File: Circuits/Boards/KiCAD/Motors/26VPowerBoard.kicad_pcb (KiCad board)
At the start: 2 copper layers, 30.5 x 25.4 mm, 13 parts, among them J1 Conn_01x01, J2 Conn_01x01, J3 Conn_01x01, U1 HCPL063

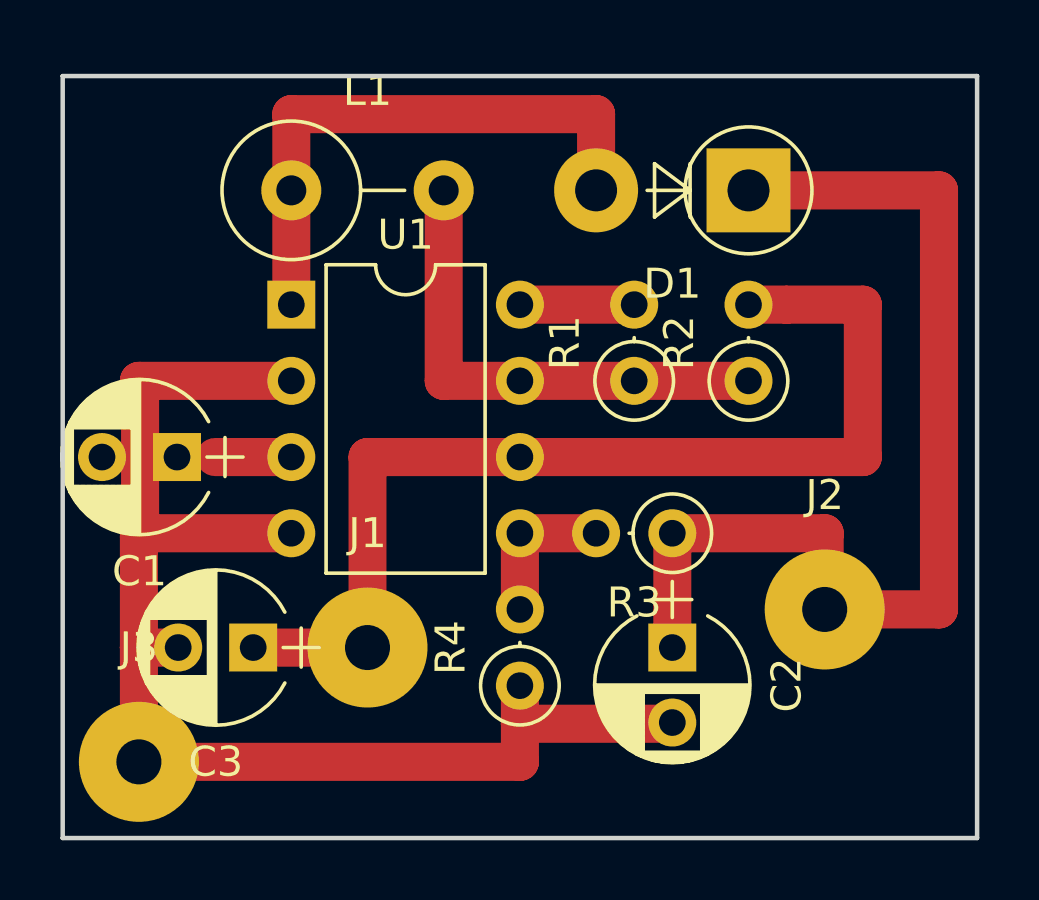
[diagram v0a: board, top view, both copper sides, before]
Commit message: Added 26V and 5V units to the Dual motor controller board
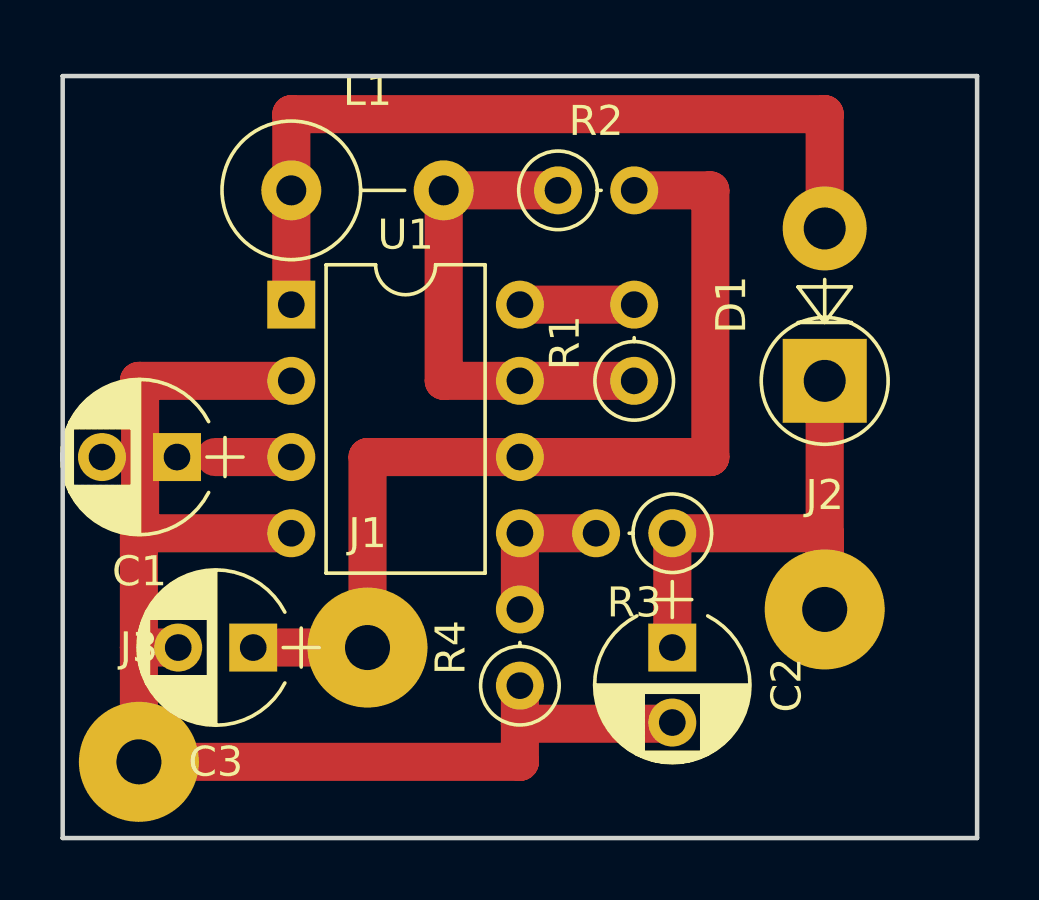
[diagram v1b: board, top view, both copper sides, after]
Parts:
- moved R2 8.98 mm to (120.7, 100.3), turned to 0 degrees
- moved D1 6.84 mm to (129.5, 106.7), turned to 90 degrees
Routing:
- net /VG2: track 35.6 -> 19.0 mm
- net /N$5: track 19.0 -> 27.9 mm
- net /VDD: track 35.6 -> 33.0 mm
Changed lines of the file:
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@@
     (links 21)
     (no_connects 2)
-    (area 104.064999 96.444999 134.695001 121.995001)
+    (area 101.344981 96.0926 134.695001 124.2174)
     (thickness 1.6)
     (drawings 4)
-    (tracks 39)
+    (tracks 36)
     (zones 0)
     (modules 13)
@@
   )
   (setup
-    (last_trace_width 0.8128)
+    (last_trace_width 1.27)
     (user_trace_width 0.1524)
     (user_trace_width 0.8128)
@@
   )
   (module Diodes_THT:D_5W_P5.08mm_Vertical_AnodeUp (layer Top)
-    (at 127 100.33 180)
+    (at 129.54 106.68 90)
     (descr "D, 5W series, Axial, Vertical, pin pitch=5.08mm, , length*diameter=8.9*3.7mm^2, , http://www.diodes.com/_files/packages/8686949.gif")
     (tags "D 5W series Axial Vertical pin pitch 5.08mm  length 8.9mm diameter 3.7mm")
-    (fp_text reference D1 (at 2.54 -3.114899 180) (layer F.SilkS)
-      (effects (font (size 1 1) (thickness 0.15)))
-    )
-    (fp_text value D (at 2.54 3.114899 180) (layer F.Fab)
-      (effects (font (size 1 1) (thickness 0.15)))
-    )
-    (fp_text user K (at -2.814899 0 180) (layer F.Fab)
-      (effects (font (size 1 1) (thickness 0.15)))
-    )
-    (fp_text user %R (at 2.54 0 180) (layer F.Fab)
+    (fp_text reference D1 (at 2.54 -3.114899 90) (layer F.SilkS)
+      (effects (font (size 1 1) (thickness 0.15)))
+    )
+    (fp_text value D (at 2.54 3.114899 90) (layer F.Fab)
+      (effects (font (size 1 1) (thickness 0.15)))
+    )
+    (fp_text user K (at -2.814899 0 90) (layer F.Fab)
+      (effects (font (size 1 1) (thickness 0.15)))
+    )
+    (fp_text user %R (at 2.54 0 90) (layer F.Fab)
       (effects (font (size 1 1) (thickness 0.15)))
     )
@@
     (fp_circle (center 0 0) (end 1.85 0) (layer F.Fab) (width 0.1))
     (fp_circle (center 0 0) (end 2.114899 0) (layer F.SilkS) (width 0.12))
-    (pad 1 thru_hole rect (at 0 0 180) (size 2.8 2.8) (drill 1.4) (layers *.Cu *.Mask)
+    (pad 1 thru_hole rect (at 0 0 90) (size 2.8 2.8) (drill 1.4) (layers *.Cu *.Mask)
       (net 3 /VG2))
-    (pad 2 thru_hole oval (at 5.08 0 180) (size 2.8 2.8) (drill 1.4) (layers *.Cu *.Mask)
+    (pad 2 thru_hole oval (at 5.08 0 90) (size 2.8 2.8) (drill 1.4) (layers *.Cu *.Mask)
       (net 4 /N$5))
     (model ${KISYS3DMOD}/Diodes_THT.3dshapes/D_5W_P5.08mm_Vertical_AnodeUp.wrl
@@
   )
   (module Resistors_THT:R_Axial_DIN0207_L6.3mm_D2.5mm_P2.54mm_Vertical (layer Top)
-    (at 127 106.68 90)
+    (at 120.65 100.33)
     (descr "Resistor, Axial_DIN0207 series, Axial, Vertical, pin pitch=2.54mm, 0.25W = 1/4W, length*diameter=6.3*2.5mm^2, http://cdn-reichelt.de/documents/datenblatt/B400/1_4W%23YAG.pdf")
     (tags "Resistor Axial_DIN0207 series Axial Vertical pin pitch 2.54mm 0.25W = 1/4W length 6.3mm diameter 2.5mm")
-    (fp_text reference R2 (at 1.27 -2.31 90) (layer F.SilkS)
-      (effects (font (size 1 1) (thickness 0.15)))
-    )
-    (fp_text value 0.22 (at 1.27 2.31 90) (layer F.Fab)
+    (fp_text reference R2 (at 1.27 -2.31) (layer F.SilkS)
+      (effects (font (size 1 1) (thickness 0.15)))
+    )
+    (fp_text value 0.22 (at 1.27 2.31) (layer F.Fab)
       (effects (font (size 1 1) (thickness 0.15)))
     )
@@
     (fp_line (start 3.65 1.6) (end 3.65 -1.6) (layer F.CrtYd) (width 0.05))
     (fp_line (start 3.65 -1.6) (end -1.6 -1.6) (layer F.CrtYd) (width 0.05))
-    (pad 1 thru_hole circle (at 0 0 90) (size 1.6 1.6) (drill 0.889) (layers *.Cu *.Mask)
+    (pad 1 thru_hole circle (at 0 0) (size 1.6 1.6) (drill 0.889) (layers *.Cu *.Mask)
       (net 5 /N$12))
-    (pad 2 thru_hole oval (at 2.54 0 90) (size 1.6 1.6) (drill 0.889) (layers *.Cu *.Mask)
+    (pad 2 thru_hole oval (at 2.54 0) (size 1.6 1.6) (drill 0.889) (layers *.Cu *.Mask)
       (net 7 /VDD))
     (model ${KISYS3DMOD}/Resistors_THT.3dshapes/R_Axial_DIN0207_L6.3mm_D2.5mm_P2.54mm_Vertical.wrl
@@
   (segment (start 106.68 106.68) (end 106.72 106.72) (width 1.27) (layer Top) (net 2))
   (segment (start 124.42 118.11) (end 124.46 118.07) (width 1.27) (layer Top) (net 2) (status 30))
-  (segment (start 127 100.33) (end 133.35 100.33) (width 1.27) (layer Top) (net 3) (status 10))
-  (segment (start 133.35 114.3) (end 129.54 114.3) (width 1.27) (layer Top) (net 3))
-  (segment (start 133.35 100.33) (end 133.35 114.3) (width 1.27) (layer Top) (net 3))
+  (segment (start 129.54 106.68) (end 129.54 114.3) (width 1.27) (layer Top) (net 3) (status C00000))
   (segment (start 129.54 114.3) (end 129.54 111.76) (width 1.27) (layer Top) (net 3))
   (segment (start 124.46 111.76) (end 129.54 111.76) (width 1.27) (layer Top) (net 3))
   (segment (start 124.46 111.76) (end 124.46 115.57) (width 1.27) (layer Top) (net 3))
-  (segment (start 111.76 100.33) (end 111.76 97.79) (width 1.27) (layer Top) (net 4))
-  (segment (start 121.92 97.79) (end 121.92 100.33) (width 1.27) (layer Top) (net 4))
-  (segment (start 111.76 97.79) (end 121.92 97.79) (width 1.27) (layer Top) (net 4))
+  (segment (start 111.76 100.33) (end 111.76 97.79) (width 1.27) (layer Top) (net 4) (status 400000))
+  (segment (start 129.54 97.79) (end 129.54 101.6) (width 1.27) (layer Top) (net 4) (status 800000))
+  (segment (start 111.76 97.79) (end 129.54 97.79) (width 1.27) (layer Top) (net 4))
   (segment (start 111.76 104.14) (end 111.76 100.33) (width 1.27) (layer Top) (net 4) (status 20))
+  (segment (start 116.84 100.33) (end 120.65 100.33) (width 1.27) (layer Top) (net 5) (status C00000))
   (segment (start 116.84 100.33) (end 116.84 106.68) (width 1.27) (layer Top) (net 5))
   (segment (start 116.84 106.68) (end 119.38 106.68) (width 1.27) (layer Top) (net 5))
   (segment (start 119.38 106.68) (end 123.19 106.68) (width 1.27) (layer Top) (net 5))
-  (segment (start 127 106.68) (end 123.19 106.68) (width 1.27) (layer Top) (net 5))
   (segment (start 123.19 104.14) (end 119.38 104.14) (width 1.27) (layer Top) (net 6))
+  (segment (start 123.19 100.33) (end 125.73 100.33) (width 1.27) (layer Top) (net 7) (status 400000))
+  (segment (start 125.73 109.22) (end 119.38 109.22) (width 1.27) (layer Top) (net 7) (status 800000))
+  (segment (start 125.73 100.33) (end 125.73 109.22) (width 1.27) (layer Top) (net 7))
   (segment (start 110.49 115.57) (end 114.3 115.57) (width 1.27) (layer Top) (net 7))
   (segment (start 119.38 109.22) (end 114.3 109.22) (width 1.27) (layer Top) (net 7))
   (segment (start 114.3 109.22) (end 114.3 115.57) (width 1.27) (layer Top) (net 7) (status 20))
-  (segment (start 119.38 109.22) (end 130.81 109.22) (width 1.27) (layer Top) (net 7))
-  (segment (start 130.81 104.14) (end 128.27 104.14) (width 1.27) (layer Top) (net 7))
-  (segment (start 130.81 109.22) (end 130.81 104.14) (width 1.27) (layer Top) (net 7))
-  (segment (start 127 104.14) (end 128.27 104.14) (width 1.27) (layer Top) (net 7))
   (segment (start 119.38 111.76) (end 119.38 114.3) (width 1.27) (layer Top) (net 8))
   (segment (start 119.38 111.76) (end 121.92 111.76) (width 1.27) (layer Top) (net 8))
